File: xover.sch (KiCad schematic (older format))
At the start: 29 parts

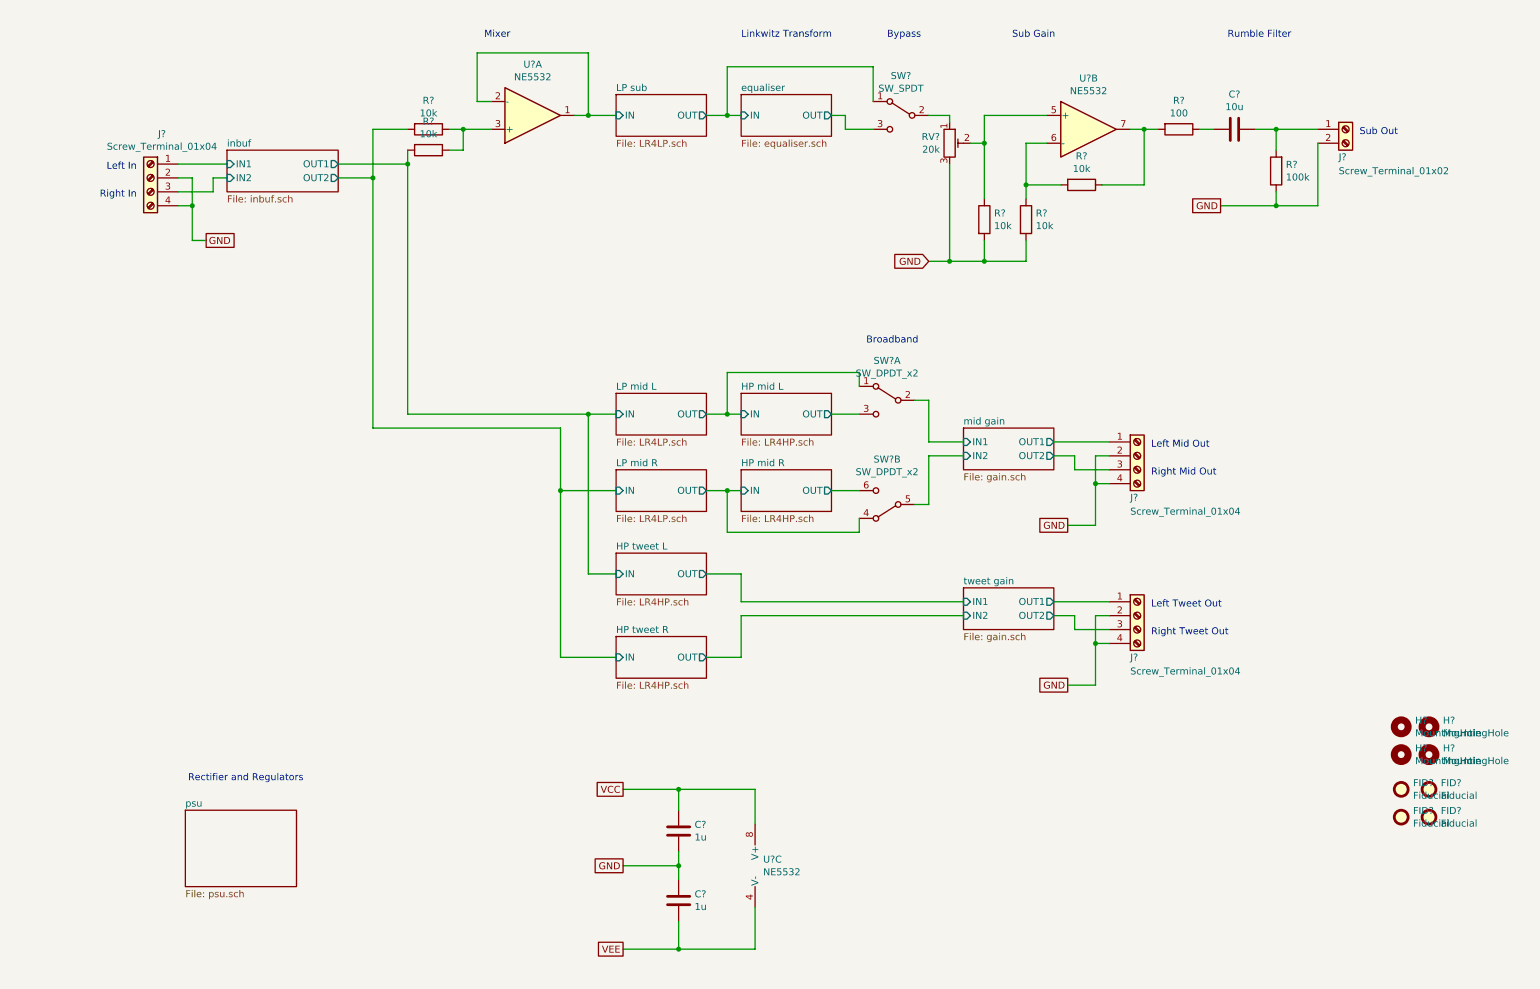
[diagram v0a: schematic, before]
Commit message: adjusted some caps in PSU and rumble filter
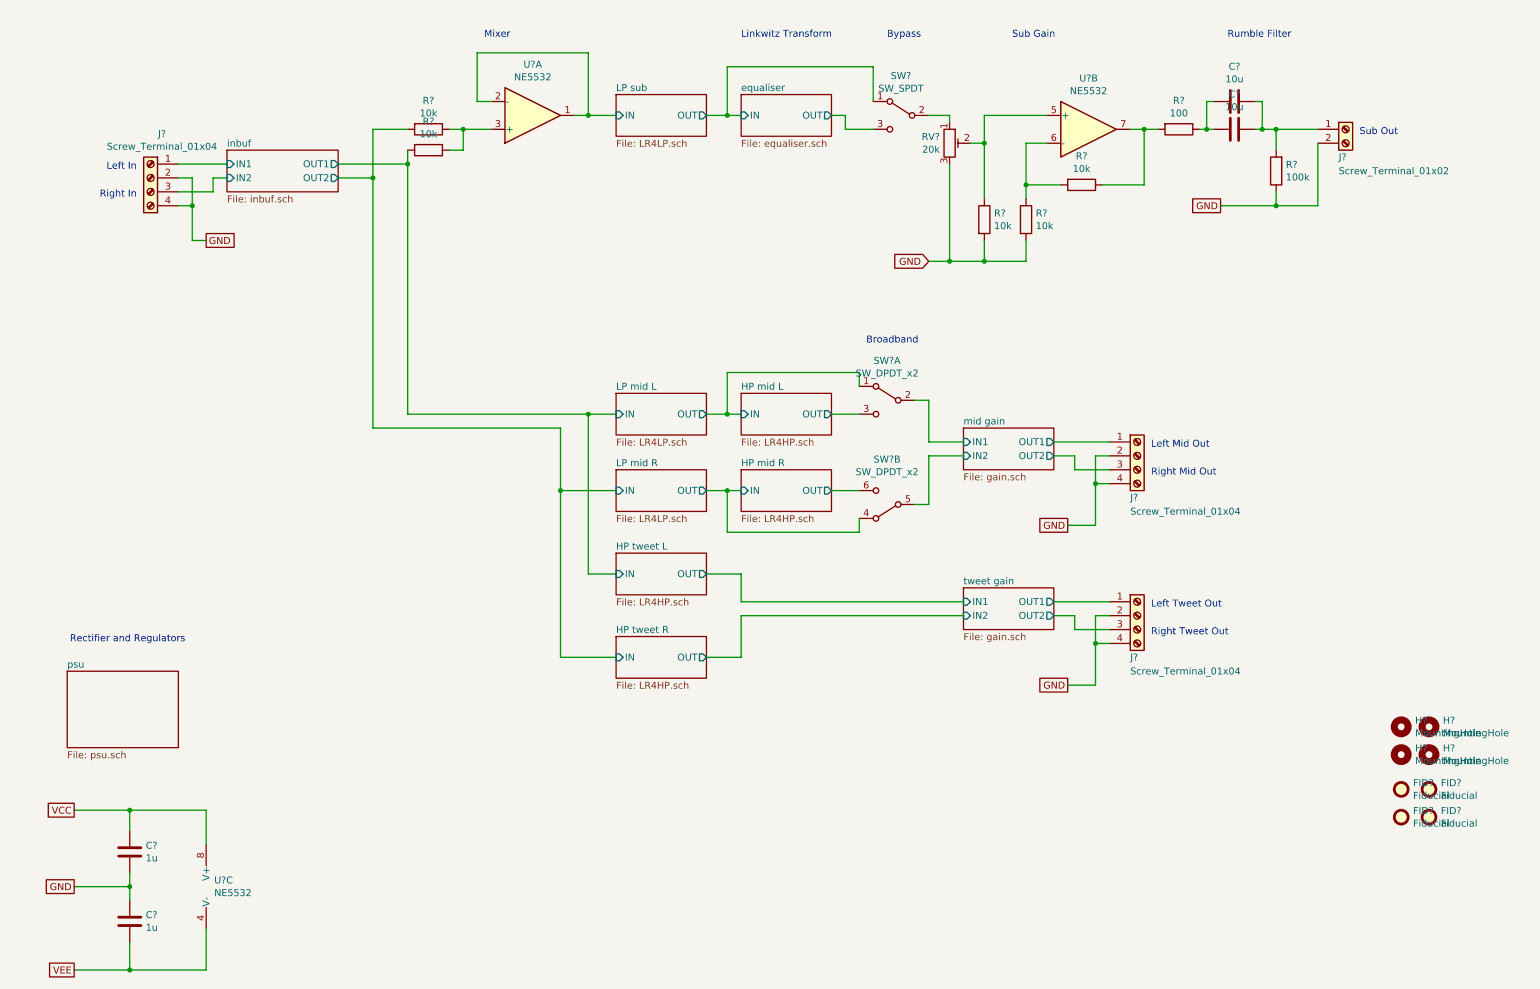
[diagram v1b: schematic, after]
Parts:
- added C?: 10u, Capacitors_ThroughHole:C_Rect_L18.0mm_W11.0mm_P15.00mm_FKS3_FKP3, symbol Device:C
- C?: footprint Capacitors_ThroughHole:CP_Radial_D6.3mm_P2.50mm -> Capacitors_SMD:C_0805
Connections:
- net at C?.2, R?.1: now also C?.2
- net at C?.1, J?.1 (Pin_1), R?.2: now also C?.1
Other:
- moved on the sheet: C?, U?C
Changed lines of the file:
@@
 L Amplifier_Operational:NE5532 U?
 U 3 1 615F8851
-P 5900 6750
-F 0 "U?" H 5858 6796 50  0000 L CNN
-F 1 "NE5532" H 5858 6705 50  0000 L CNN
-F 2 "" H 5900 6750 50  0001 C CNN
-F 3 "http://www.ti.com/lit/ds/symlink/ne5532.pdf" H 5900 6750 50  0001 C CNN
-	3    5900 6750
+P 1950 6900
+F 0 "U?" H 1908 6946 50  0000 L CNN
+F 1 "NE5532" H 1908 6855 50  0000 L CNN
+F 2 "" H 1950 6900 50  0001 C CNN
+F 3 "http://www.ti.com/lit/ds/symlink/ne5532.pdf" H 1950 6900 50  0001 C CNN
+	3    1950 6900
 	1    0    0    -1
 $EndComp
@@
 L Device:C C?
 U 1 1 615FF758
-P 5250 7000
+P 1300 7150
 AR Path="/6157B871/615FF758" Ref="C?"  Part="1"
 AR Path="/615961F1/615FF758" Ref="C?"  Part="1"
@@
 AR Path="/615C4B54/615FF758" Ref="C?"  Part="1"
 AR Path="/615FF758" Ref="C?"  Part="1"
-F 0 "C?" H 5365 7046 50  0000 L CNN
-F 1 "1u" H 5365 6955 50  0000 L CNN
-F 2 "Capacitors_SMD:C_0805" H 5288 6850 50  0001 C CNN
-F 3 "~" H 5250 7000 50  0001 C CNN
-	1    5250 7000
+F 0 "C?" H 1415 7196 50  0000 L CNN
+F 1 "1u" H 1415 7105 50  0000 L CNN
+F 2 "Capacitors_SMD:C_0805" H 1338 7000 50  0001 C CNN
+F 3 "~" H 1300 7150 50  0001 C CNN
+	1    1300 7150
 	1    0    0    -1
 $EndComp
@@
 L Device:C C?
 U 1 1 615FF75E
-P 5250 6500
+P 1300 6650
 AR Path="/6157B871/615FF75E" Ref="C?"  Part="1"
 AR Path="/615961F1/615FF75E" Ref="C?"  Part="1"
@@
 AR Path="/615C4B54/615FF75E" Ref="C?"  Part="1"
 AR Path="/615FF75E" Ref="C?"  Part="1"
-F 0 "C?" H 5365 6546 50  0000 L CNN
-F 1 "1u" H 5365 6455 50  0000 L CNN
-F 2 "Capacitors_SMD:C_0805" H 5288 6350 50  0001 C CNN
-F 3 "~" H 5250 6500 50  0001 C CNN
-	1    5250 6500
-	1    0    0    -1
-$EndComp
-Wire Wire Line
-	5250 6650 5250 6750
-Connection ~ 5250 6750
-Wire Wire Line
-	5250 6750 5250 6850
-Text GLabel 4850 6750 0    50   UnSpc ~ 0
+F 0 "C?" H 1415 6696 50  0000 L CNN
+F 1 "1u" H 1415 6605 50  0000 L CNN
+F 2 "Capacitors_SMD:C_0805" H 1338 6500 50  0001 C CNN
+F 3 "~" H 1300 6650 50  0001 C CNN
+	1    1300 6650
+	1    0    0    -1
+$EndComp
+Wire Wire Line
+	1300 6800 1300 6900
+Connection ~ 1300 6900
+Wire Wire Line
+	1300 6900 1300 7000
+Text GLabel 900  6900 0    50   UnSpc ~ 0
 GND
-Text GLabel 4850 6200 0    50   UnSpc ~ 0
+Text GLabel 900  6350 0    50   UnSpc ~ 0
 VCC
-Text GLabel 4850 7350 0    50   UnSpc ~ 0
+Text GLabel 900  7500 0    50   UnSpc ~ 0
 VEE
 Wire Wire Line
-	4850 6200 5250 6200
-Wire Wire Line
-	5250 6200 5250 6350
-Wire Wire Line
-	4850 7350 5250 7350
-Wire Wire Line
-	5250 7350 5250 7150
-Wire Wire Line
-	5250 6200 5800 6200
-Connection ~ 5250 6200
-Wire Wire Line
-	5250 7350 5800 7350
-Connection ~ 5250 7350
-Wire Wire Line
-	5800 6200 5800 6450
-Wire Wire Line
-	5800 7050 5800 7350
+	900  6350 1300 6350
+Wire Wire Line
+	1300 6350 1300 6500
+Wire Wire Line
+	900  7500 1300 7500
+Wire Wire Line
+	1300 7500 1300 7300
+Wire Wire Line
+	1300 6350 1850 6350
+Connection ~ 1300 6350
+Wire Wire Line
+	1300 7500 1850 7500
+Connection ~ 1300 7500
+Wire Wire Line
+	1850 6350 1850 6600
+Wire Wire Line
+	1850 7200 1850 7500
 Wire Wire Line
 	5700 4650 5700 4850
@@
 F 0 "C?" V 8998 1450 50  0000 C CNN
 F 1 "10u" V 9089 1450 50  0000 C CNN
-F 2 "Capacitors_ThroughHole:CP_Radial_D6.3mm_P2.50mm" H 9288 1300 50  0001 C CNN
+F 2 "Capacitors_SMD:C_0805" H 9288 1300 50  0001 C CNN
 F 3 "~" H 9250 1450 50  0001 C CNN
 	1    9250 1450
@@
 Connection ~ 8600 1450
 Wire Wire Line
-	9000 1450 9100 1450
-Wire Wire Line
-	9400 1450 9550 1450
+	9000 1450 9050 1450
+Wire Wire Line
+	9400 1450 9450 1450
 Wire Wire Line
 	9550 1450 9550 1600
@@
 Right In
 Wire Wire Line
-	4850 6750 5250 6750
+	900  6900 1300 6900
 $Sheet
-S 1700 6350 800  550
+S 850  5350 800  550
 U 61A2CF17
 F0 "psu" 50
 F1 "psu.sch" 50
 $EndSheet
-Text Notes 2550 6150 2    50   ~ 0
+Text Notes 1700 5150 2    50   ~ 0
 Rectifier and Regulators
+$Comp
+L Device:C C?
+U 1 1 615E0126
+P 9250 1250
+AR Path="/616914EE/615E0126" Ref="C?"  Part="1"
+AR Path="/615E0126" Ref="C?"  Part="1"
+F 0 "C?" V 8998 1250 50  0000 C CNN
+F 1 "10u" V 9089 1250 50  0000 C CNN
+F 2 "Capacitors_ThroughHole:C_Rect_L18.0mm_W11.0mm_P15.00mm_FKS3_FKP3" H 9288 1100 50  0001 C CNN
+F 3 "~" H 9250 1250 50  0001 C CNN
+	1    9250 1250
+	0    1    1    0
+$EndComp
+Wire Wire Line
+	9100 1250 9050 1250
+Wire Wire Line
+	9050 1250 9050 1450
+Connection ~ 9050 1450
+Wire Wire Line
+	9050 1450 9100 1450
+Wire Wire Line
+	9400 1250 9450 1250
+Wire Wire Line
+	9450 1250 9450 1450
+Connection ~ 9450 1450
+Wire Wire Line
+	9450 1450 9550 1450
 $EndSCHEMATC

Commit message: improved PSU, gain up front, reordered filter stages, shrunk rumble filter
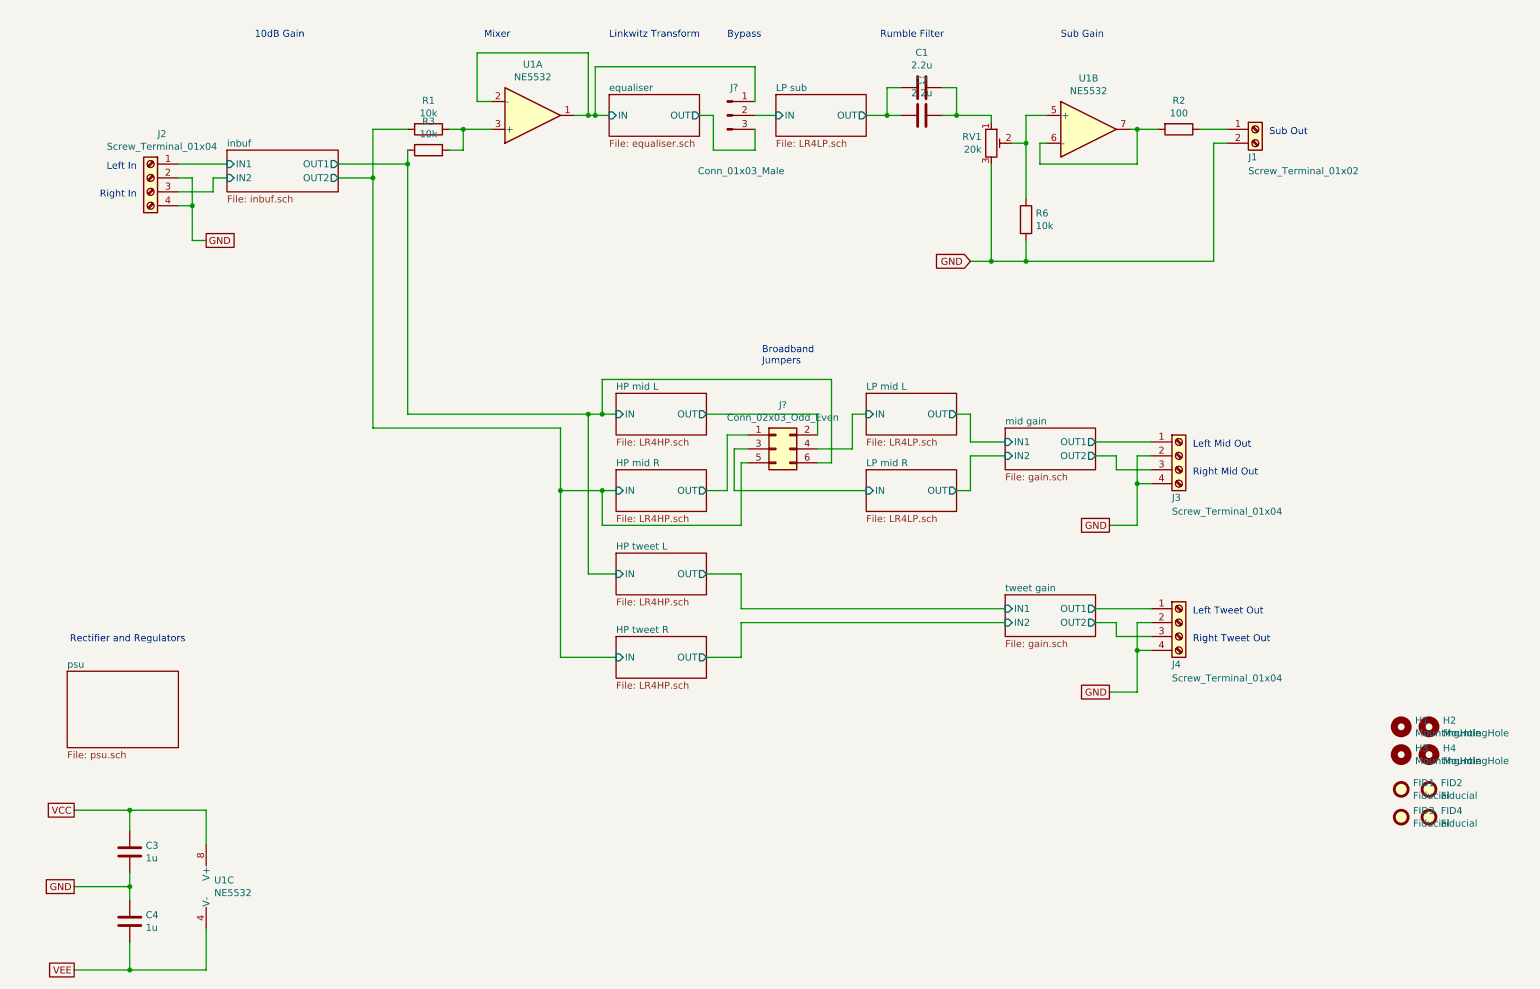
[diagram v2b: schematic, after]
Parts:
- removed R? (x2): 10k, Resistors_SMD:R_0805, symbol Device:R
- removed R?: 100k, Resistors_SMD:R_0805, symbol Device:R
- removed SW? (x2): SW_DPDT_x2, symbol Switch:SW_DPDT_x2
- removed SW?: SW_SPDT, symbol Switch:SW_SPDT
- added J?: Conn_02x03_Odd_Even, Pin_Headers:Pin_Header_Straight_2x03_Pitch2.54mm, symbol Connector_Generic:Conn_02x03_Odd_Even
- added J?: Conn_01x03_Male, Pin_Headers:Pin_Header_Straight_1x03_Pitch2.54mm, symbol Connector:Conn_01x03_Male
- C1, C2: renamed from C?; value 10u -> 2.2u
- J1: renamed from J?; footprint (none) -> Terminals_Phoenix:TerminalBlock_Phoenix_MPT-2.54mm_2pol
- J2, J3, J4: renamed from J?; footprint (none) -> Terminals_Phoenix:TerminalBlock_Phoenix_MPT-2.54mm_4pol
- U1: renamed from U?; footprint (none) -> Housings_DIP:DIP-8_W7.62mm_Socket
- gave numbers to parts that had none: 15
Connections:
- net HP tweet L/IN is gone; now on net HP mid L/IN: R3.2
- net HP tweet R/IN is gone; now on net HP mid R/IN: R1.2
- net HP mid L/IN: now also J?.6 (Pin_6)
- net HP mid L/OUT: now also J?.2 (Pin_2)
- net HP mid R/IN: now also J?.5 (Pin_5)
- net HP mid R/OUT: now also J?.1 (Pin_1)
- net LP sub/IN: now also J?.2 (Pin_2); no longer U1.1, U1.2 (-)
- net LP sub/OUT: now also C1.2, C2.2
- net equaliser/OUT: now also J?.3 (Pin_3)
- net at C1.1, C2.1: now also RV1.1; no longer J1.1 (Pin_1)
- net at U1.6 (-): now also R2.2, U1.7
- new net: J1.1 (Pin_1), R2.1
- new net LP mid L/IN: J?.4 (Pin_4)
- new net LP mid R/IN: J?.3 (Pin_3)
- new net equaliser/IN: J?.1 (Pin_1), U1.1, U1.2 (-)
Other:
- note added: "10dB Gain"
- note added: "Broadband\nJumpers"
- note removed: "Broadband"
- moved on the sheet: C1, C2, J1, J3, J4, R6, RV1

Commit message: added buffered volume pot, and fixed subsonic filter added signal taps for external transforms/filters to be added later
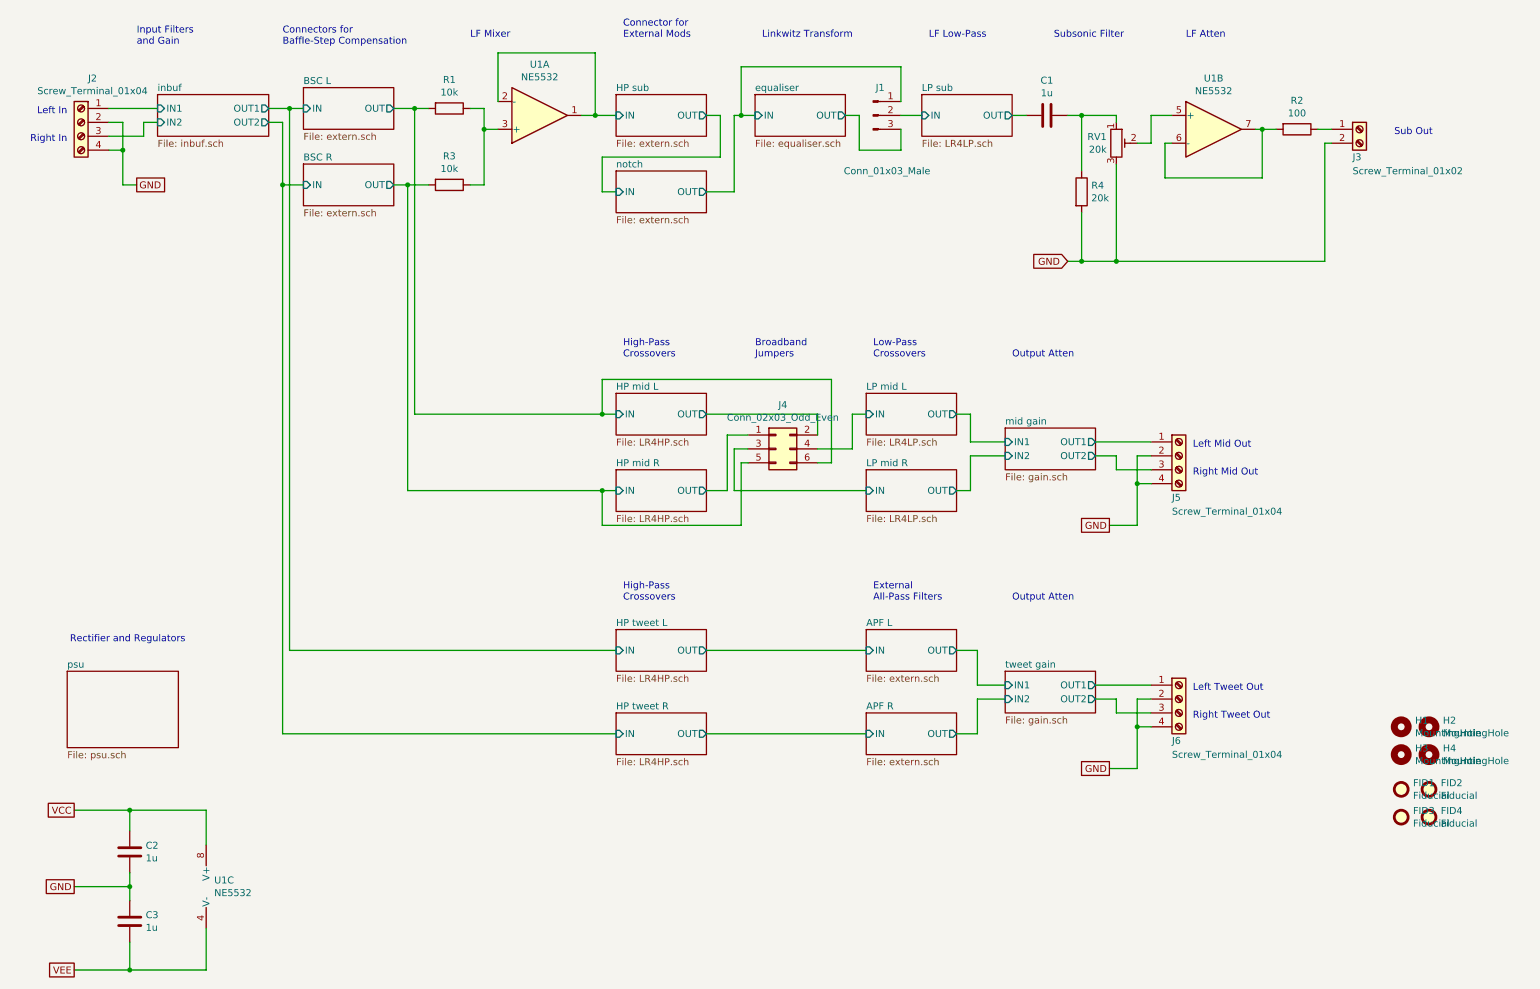
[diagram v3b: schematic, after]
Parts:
- removed C2: 2.2u, Capacitors_SMD:C_0805, symbol Device:C
- C1: value 2.2u -> 1u; footprint Capacitors_ThroughHole:C_Rect_L18.0mm_W11.0mm_P15.00mm_FKS3_FKP3 -> Capacitors_ThroughHole:C_Rect_L7.2mm_W7.2mm_P5.00mm_FKS2_FKP2_MKS2_MKP2
- R4: renamed from R6; value 10k -> 20k
- gave numbers to parts that had none: 2
- renumbered C3 to C2, C4 to C3, J1 to J3, J3 to J5, J4 to J6
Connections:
- net equaliser/IN: no longer U1.1, U1.2 (-)
- net at C1.1, RV1.1: now also R4.1
- net at RV1.2, U1.5 (+): no longer R4.1
- net HP mid L/IN renamed BSC L/OUT
- net BSC L/OUT: now also R1.2; no longer R3.2
- net HP mid R/IN renamed BSC R/OUT
- net BSC R/OUT: now also R3.2; no longer R1.2
- new net HP sub/IN: U1.1, U1.2 (-)
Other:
- note added: "Connector for\nExternal Mods"
- note added: "Connectors for\nBaffle-Step Compensation"
- note added: "External\nAll-Pass Filters"
- note added: "High-Pass\nCrossovers"
- note added: "Input Filters\nand Gain"
- note added: "LF Atten"
- note added: "LF Low-Pass"
- note added: "LF Mixer"
- note added: "Low-Pass\nCrossovers"
- note added: "Output Atten"
- note added: "Subsonic Filter"
- note removed: "10dB Gain"
- note removed: "Bypass"
- note removed: "Mixer"
- note removed: "Rumble Filter"
- note removed: "Sub Gain"
- moved on the sheet: C1, J1, J2, J3, J6, R1, R2, R3, R4, RV1, U1A, U1B
